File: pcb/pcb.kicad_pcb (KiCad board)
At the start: 2 copper layers, 100 x 88.7 mm, 65 parts, among them J1 AudioJack4, J2 USB_C_Receptacle_USB2.0, SW1 Switch, SW10 Switch, SW11 Switch, SW12 Switch, SW13 Switch, SW14 Switch, SW15 Switch, SW16 Switch, SW17 Switch, SW18 Switch, SW2 Switch, SW3 Switch, SW4 Switch, SW5 Switch, SW6 Switch, SW7 Switch, SW8 Switch, SW9 Switch, U1 MCU_rp2040-zero, U2 MCU_rp2040-zero, U3 RollerEncoder_EVQWGD001

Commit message: v2
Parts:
- removed the D17 at (102.5, 106.0)
- removed D19: D_Small, zzkeeb:Diode_1N4148-SOD123-reversible-flip3d
- removed H1, H2, H3, H4: MountingHole, zzkeeb:Hole_M2-spacer
- removed J2: USB_C_Receptacle_USB2.0, zzkeeb:Connector_USB-C-mid-mount-ali-reversible-data
- removed the LED16 at (102.5, 109.8)
- removed RE1: RotaryEncoder_Switch, zzkeeb:RotaryEncoder_EC11-reversible
- removed the SW16 at (102.5, 114.5)
- removed U3: RollerEncoder_EVQWGD001, zzkeeb:RotaryEncoder_EVQWGD001
- added D18: Diode, zzkeeb:Diode_1N4148-SOD123-reversible-flip3d, B.Cu at (103.5, 105.0)
- added FiveWay1: 5Way-Tactile_K1-1506DN-01, zzkeeb:Button_5way-reversible, F.Cu at (103.5, 115.5)
- added REF**: KiCad-Logo2_5mm_SilkScreen, Symbol:KiCad-Logo2_5mm_SilkScreen, F.Cu at (63.5, 47.5)
- added REF**: Logo_QMK-silkscreen, zzkeeb:Logo_QMK-silkscreen, B.Cu at (63.5, 47.5)
- added Ref**: Val**, zzkeeb:Hole_M2, F.Cu at (68.5, 43.1)
- added Ref**: Val**, zzkeeb:Hole_M2, F.Cu at (126.5, 43.1)
- added Ref**: Val**, zzkeeb:Hole_M2, F.Cu at (148.9, 107.2)
- added Ref**: Val**, zzkeeb:Hole_M2, F.Cu at (82.5, 122.4)
- added USB1: Connector_HRO-TYPE-C-31-M-12, zzkeeb:Connector_HRO-TYPE-C-31-M-12-data, F.Cu at (117.5, 39.5)
- added USB2: Connector_HRO-TYPE-C-31-M-12, zzkeeb:Connector_HRO-TYPE-C-31-M-12-data, B.Cu at (117.5, 39.5)
- D1: renamed from D5; value D_Small -> Diode
- D10: renamed from D9; value D_Small -> Diode
- D11: renamed from D15; value D_Small -> Diode
- D12: renamed from D11; value D_Small -> Diode
- D13: renamed from D12; value D_Small -> Diode
- D14: renamed from D13; value D_Small -> Diode
- D15: renamed from D14; value D_Small -> Diode
- D16: renamed from D18; value D_Small -> Diode
- D17: renamed from D16; value D_Small -> Diode
- D2: renamed from D1; value D_Small -> Diode
- D3: renamed from D2; value D_Small -> Diode
- D4: renamed from D3; value D_Small -> Diode
- D5: renamed from D4; value D_Small -> Diode
- D6: renamed from D10; value D_Small -> Diode
- D7: renamed from D6; value D_Small -> Diode
- D8: renamed from D7; value D_Small -> Diode
- D9: renamed from D8; value D_Small -> Diode
- LED1: renamed from LED17; footprint zzkeeb:LED_SK6812-MINI-E-reversible -> zzkeeb:LED_SK6812-MINI-E-reversible-flip3d
- LED10: renamed from LED7; footprint zzkeeb:LED_SK6812-MINI-E-reversible -> zzkeeb:LED_SK6812-MINI-E-reversible-flip3d
- LED11: renamed from LED2; footprint zzkeeb:LED_SK6812-MINI-E-reversible -> zzkeeb:LED_SK6812-MINI-E-reversible-flip3d
- LED12: renamed from LED1; footprint zzkeeb:LED_SK6812-MINI-E-reversible -> zzkeeb:LED_SK6812-MINI-E-reversible-flip3d
- LED13: renamed from LED6; footprint zzkeeb:LED_SK6812-MINI-E-reversible -> zzkeeb:LED_SK6812-MINI-E-reversible-flip3d
- LED14: renamed from LED11; footprint zzkeeb:LED_SK6812-MINI-E-reversible -> zzkeeb:LED_SK6812-MINI-E-reversible-flip3d
- LED15: footprint zzkeeb:LED_SK6812-MINI-E-reversible -> zzkeeb:LED_SK6812-MINI-E-reversible-flip3d
- LED16: renamed from LED10; footprint zzkeeb:LED_SK6812-MINI-E-reversible -> zzkeeb:LED_SK6812-MINI-E-reversible-flip3d
- LED17: renamed from LED5; footprint zzkeeb:LED_SK6812-MINI-E-reversible -> zzkeeb:LED_SK6812-MINI-E-reversible-flip3d
- LED2: renamed from LED18; footprint zzkeeb:LED_SK6812-MINI-E-reversible -> zzkeeb:LED_SK6812-MINI-E-reversible-flip3d
- LED3: renamed from LED14; footprint zzkeeb:LED_SK6812-MINI-E-reversible -> zzkeeb:LED_SK6812-MINI-E-reversible-flip3d
- LED4: renamed from LED9; footprint zzkeeb:LED_SK6812-MINI-E-reversible -> zzkeeb:LED_SK6812-MINI-E-reversible-flip3d
- LED5: renamed from LED4; footprint zzkeeb:LED_SK6812-MINI-E-reversible -> zzkeeb:LED_SK6812-MINI-E-reversible-flip3d
- LED6: renamed from LED3; footprint zzkeeb:LED_SK6812-MINI-E-reversible -> zzkeeb:LED_SK6812-MINI-E-reversible-flip3d
- LED7: renamed from LED8; footprint zzkeeb:LED_SK6812-MINI-E-reversible -> zzkeeb:LED_SK6812-MINI-E-reversible-flip3d
- LED8: renamed from LED13; footprint zzkeeb:LED_SK6812-MINI-E-reversible -> zzkeeb:LED_SK6812-MINI-E-reversible-flip3d
- LED9: renamed from LED12; footprint zzkeeb:LED_SK6812-MINI-E-reversible -> zzkeeb:LED_SK6812-MINI-E-reversible-flip3d
- moved U1 62.0 mm to (65.5, 114.5), turned to -90 degrees
- moved U2 62.0 mm to (65.5, 114.5), turned to 90 degrees
- moved D17 44.7 mm to (135.5, 107.0)
- moved D11 19.4 mm to (81.5, 105.5)
- moved D1 13.2 mm to (63.5, 69.5)
- moved D6 13.2 mm to (63.5, 86.5)
- moved LED15 13.2 mm to (63.5, 90.3)
- moved LED16 13.2 mm to (63.5, 73.3)
- moved LED17 13.2 mm to (63.5, 56.3)
- moved SW1 13.2 mm to (63.5, 61.0)
- moved SW11 13.2 mm to (63.5, 95.0)
- moved SW6 13.2 mm to (63.5, 78.0)
- moved J1 3.93 mm to (144.5, 46.0)
- moved LED1 3.04 mm to (123.0, 111.5)
- moved D16 2.92 mm to (123.0, 107.5)
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- renumbered SW5 to SW1, SW9 to SW10, SW15 to SW11, SW11 to SW12, SW12 to SW13, SW13 to SW14, SW14 to SW15, SW17 to SW16, SW18 to SW17, SW1 to SW2, SW2 to SW3, SW3 to SW4, SW4 to SW5, SW10 to SW6, SW6 to SW7, SW7 to SW8, SW8 to SW9
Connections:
- net ENCB renamed row4
- D1 pad 1: row1 -> row0
- D11 pad 1: row3 -> row2
- D17 pad 2: SW_ENCA -> Net-(D17-A)
- D6 pad 1: row2 -> row1
- J1 pad T: VCC -> +5V
- LED1 pad 1: VCC -> Net-(D18-K)
- LED1 pad 2: Net-(LED16-Pad4) -> Net-(LED1-DOUT)
- LED1 pad 4: Net-(LED17-Pad4) -> LED
- LED10 pad 1: VCC -> +5V
- LED10 pad 2: Net-(LED6-Pad4) -> Net-(LED10-DOUT)
- LED10 pad 4: Net-(LED7-Pad4) -> Net-(LED10-DIN)
- LED11 pad 1: VCC -> +5V
- LED11 pad 2: Net-(LED2-Pad2) -> Net-(LED11-DOUT)
- LED11 pad 4: Net-(LED1-Pad2) -> Net-(LED10-DOUT)
- LED12 pad 1: VCC -> +5V
- LED12 pad 2: Net-(LED1-Pad2) -> Net-(LED12-DOUT)
- LED12 pad 4: LED -> Net-(LED11-DOUT)
- LED13 pad 1: VCC -> +5V
- LED13 pad 2: Net-(LED5-Pad4) -> Net-(LED13-DOUT)
- LED13 pad 4: Net-(LED6-Pad4) -> Net-(LED12-DOUT)
- LED14 pad 1: VCC -> +5V
- LED14 pad 2: Net-(LED11-Pad2) -> Net-(LED14-DOUT)
- LED14 pad 4: Net-(LED10-Pad2) -> Net-(LED13-DOUT)
- LED15 pad 1: VCC -> +5V
- LED15 pad 2: unconnected-(LED15-Pad2) -> Net-(LED15-DOUT)
- LED15 pad 4: Net-(LED15-Pad4) -> Net-(LED14-DOUT)
- LED16 pad 1: VCC -> +5V
- LED16 pad 2: Net-(LED10-Pad2) -> Net-(LED16-DOUT)
- LED16 pad 4: Net-(LED10-Pad4) -> Net-(LED15-DOUT)
- LED17 pad 1: VCC -> +5V
- LED17 pad 2: Net-(LED10-Pad4) -> unconnected-(LED17-DOUT-Pad2)
- LED17 pad 4: Net-(LED5-Pad4) -> Net-(LED16-DOUT)
- LED2 pad 1: VCC -> +5V
- LED2 pad 2: Net-(LED17-Pad4) -> Net-(LED2-DOUT)
- LED2 pad 4: Net-(LED14-Pad2) -> Net-(LED1-DOUT)
- LED3 pad 1: VCC -> +5V
- LED3 pad 2: Net-(LED14-Pad2) -> Net-(LED3-DOUT)
- LED3 pad 4: Net-(LED13-Pad2) -> Net-(LED2-DOUT)
- LED4 pad 1: VCC -> +5V
- LED4 pad 2: Net-(LED8-Pad4) -> Net-(LED4-DOUT)
- LED4 pad 4: Net-(LED4-Pad2) -> Net-(LED3-DOUT)
- LED5 pad 1: VCC -> +5V
- LED5 pad 2: Net-(LED4-Pad2) -> Net-(LED5-DOUT)
- LED5 pad 4: Net-(LED3-Pad2) -> Net-(LED4-DOUT)
- LED6 pad 1: VCC -> +5V
- LED6 pad 2: Net-(LED3-Pad2) -> Net-(LED6-DOUT)
- LED6 pad 4: Net-(LED2-Pad2) -> Net-(LED5-DOUT)
- LED7 pad 1: VCC -> +5V
- LED7 pad 2: Net-(LED7-Pad4) -> Net-(LED7-DOUT)
- LED7 pad 4: Net-(LED8-Pad4) -> Net-(LED6-DOUT)
- LED8 pad 1: VCC -> +5V
- LED8 pad 2: Net-(LED13-Pad2) -> Net-(LED8-DOUT)
- LED8 pad 4: Net-(LED12-Pad2) -> Net-(LED7-DOUT)
- LED9 pad 1: VCC -> +5V
- LED9 pad 2: Net-(LED12-Pad2) -> Net-(LED10-DIN)
- LED9 pad 4: Net-(LED11-Pad2) -> Net-(LED8-DOUT)
- SW17 pad 1: Net-(D19-Pad2) -> Net-(D17-A)
- U1 pad 17: ENCA -> unconnected-(U1-26-Pad17)
- U1 pad 21: VCC -> unconnected-(U1-3V3-Pad21)
- U2 pad 21: VCC -> unconnected-(U2-3V3-Pad21)
- U2 pad 7: ENCA -> unconnected-(U2-6-Pad7)
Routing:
- net VCC: track 635.8 -> 0.00 mm, vias 20 -> 0
- net +5V: track 0.00 -> 633.9 mm, vias 0 -> 20
- net row3: track 175.1 -> 105.3 mm, vias 6 -> 4
- net col0: track 106.6 -> 174.3 mm
- net ENCA: track 61.7 -> 0.00 mm, vias 2 -> 0
- net row2: track 149.7 -> 99.0 mm
- net row0: track 93.6 -> 142.3 mm, vias 5 -> 6
- net Net-(D17-A): track 0.00 -> 47.5 mm, vias 0 -> 2
- net Net-(LED15-Pad4): track 44.0 -> 0.00 mm, vias 2 -> 0
- net Net-(LED2-DOUT): track 0.00 -> 44.0 mm, vias 0 -> 2
- net row4: track 107.1 -> 64.8 mm
- net Net-(D17-Pad2): track 42.1 -> 0.00 mm, vias 2 -> 0
- net col2: track 210.1 -> 169.6 mm, vias 5 -> 4
- net Net-(LED14-Pad2): track 39.7 -> 0.00 mm, vias 2 -> 0
- net Net-(D19-Pad2): track 39.3 -> 0.00 mm, vias 2 -> 0
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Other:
- board size 100 x 88.7 mm -> 100 x 89 mm
- board text added: "v2.0"
- board text removed: "v1.1"

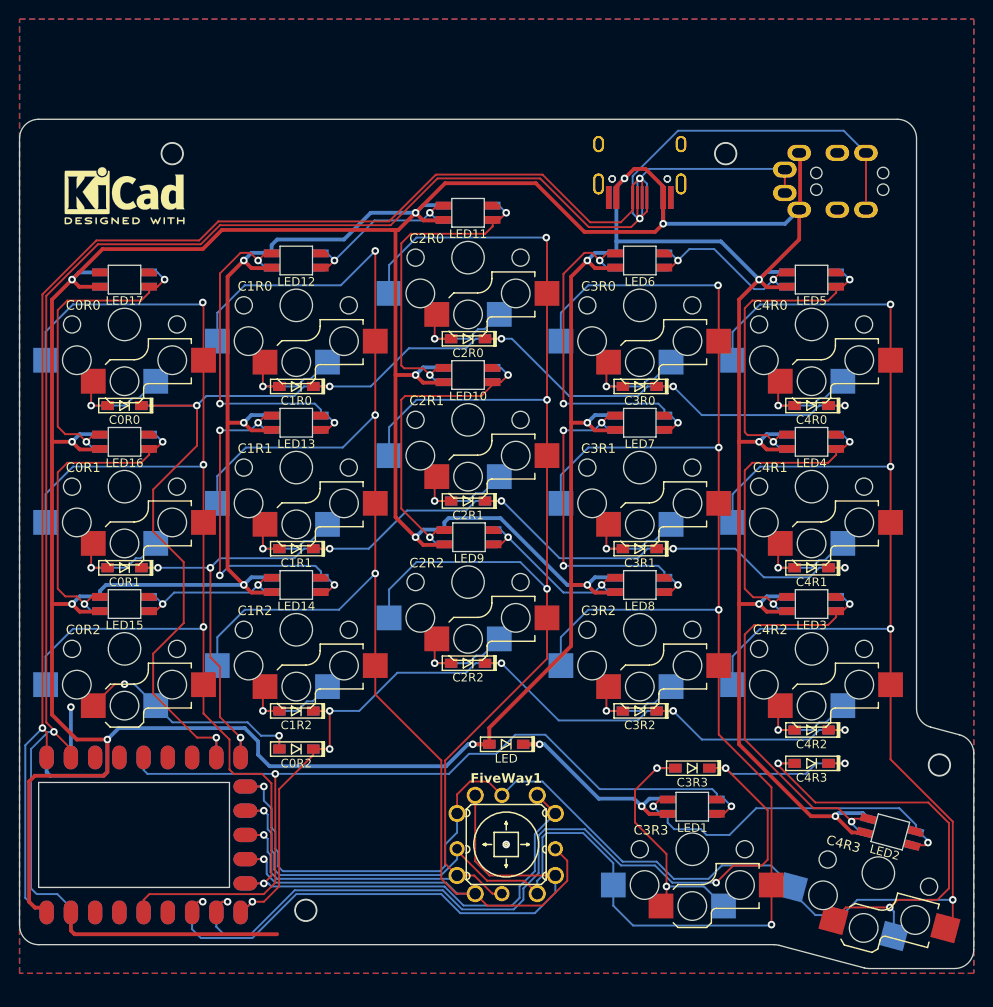
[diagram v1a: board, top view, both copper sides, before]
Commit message: use alps smd 5way
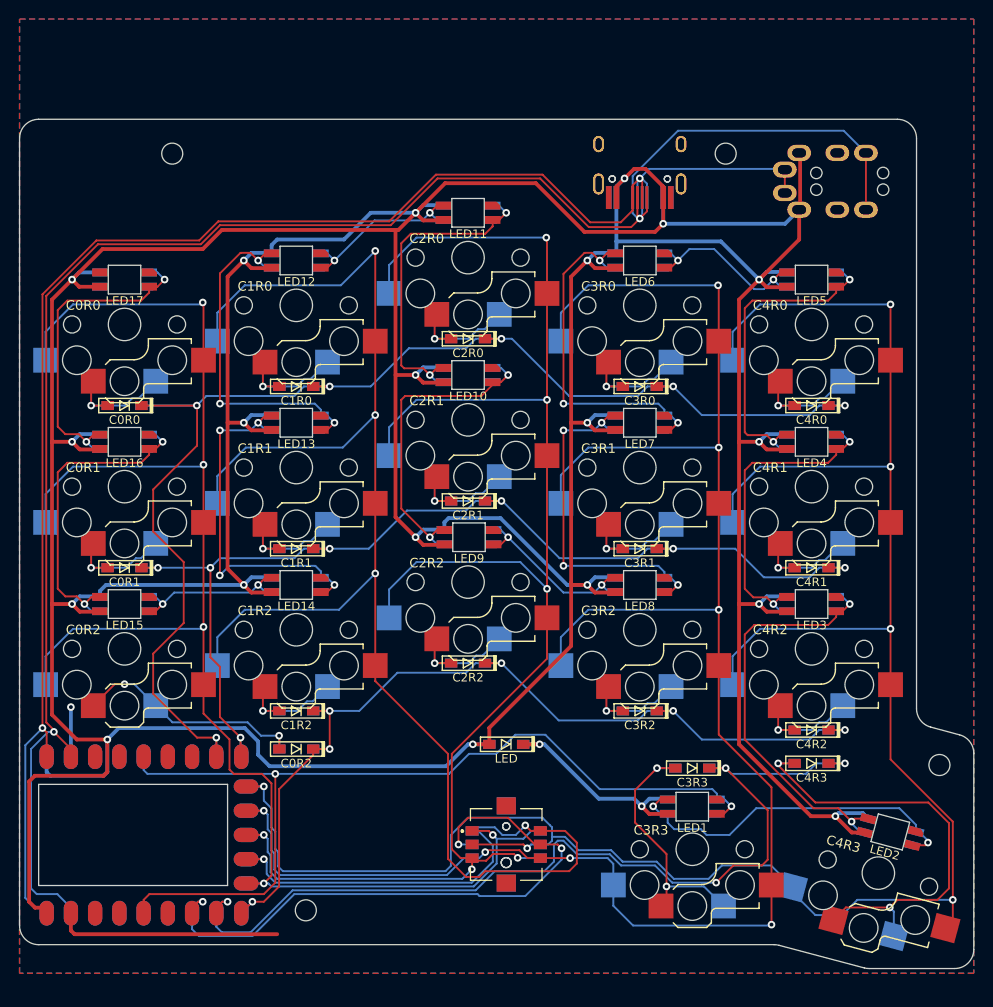
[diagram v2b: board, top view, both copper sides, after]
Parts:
- removed FiveWay1: 5Way-Tactile_K1-1506DN-01, zzkeeb:Button_5way-reversible
- removed REF**: KiCad-Logo2_5mm_SilkScreen, Symbol:KiCad-Logo2_5mm_SilkScreen
- removed REF**: Logo_QMK-silkscreen, zzkeeb:Logo_QMK-silkscreen
- removed Ref** (x4): Val**, zzkeeb:Hole_M2
- added S1: Button_5way-SKRHABE010, zzkeeb:Button_5way-SKRHABE010, F.Cu at (103.5, 115.5)
- added S2: Button_5way-SKRHABE010, zzkeeb:Button_5way-SKRHABE010, B.Cu at (103.5, 115.5)
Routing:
- net col1: track 183.8 -> 199.2 mm, vias 4 -> 5
- net col3: track 211.5 -> 202.2 mm, vias 5 -> 7
- net col0: track 174.3 -> 169.1 mm, vias 4 -> 5
- net row3: track 105.3 -> 100.5 mm
- net col2: track 169.6 -> 173.8 mm, vias 4 -> 6
- net col4: track 232.0 -> 235.8 mm, vias 5 -> 6
- net row4: track 64.8 -> 64.5 mm, vias 1 -> 3
- net GND: vias 2 -> 1
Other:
- outline, holes or cut-outs redrawn
